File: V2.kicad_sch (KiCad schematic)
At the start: 106 parts, among them J5 Conn_01x06, Q1 NMOS, Q10 NMOS, Q11 NMOS, Q12 NMOS, Q13 Q_NPN_BCE, Q2 NMOS, Q3 NMOS, Q4 NMOS, Q5 NMOS, Q6 NMOS, Q7 NMOS, Q8 NMOS, Q9 NMOS, U10 STM32F042F6Px, U8 BQ25750RRVR, U9 BQ76952PFBR

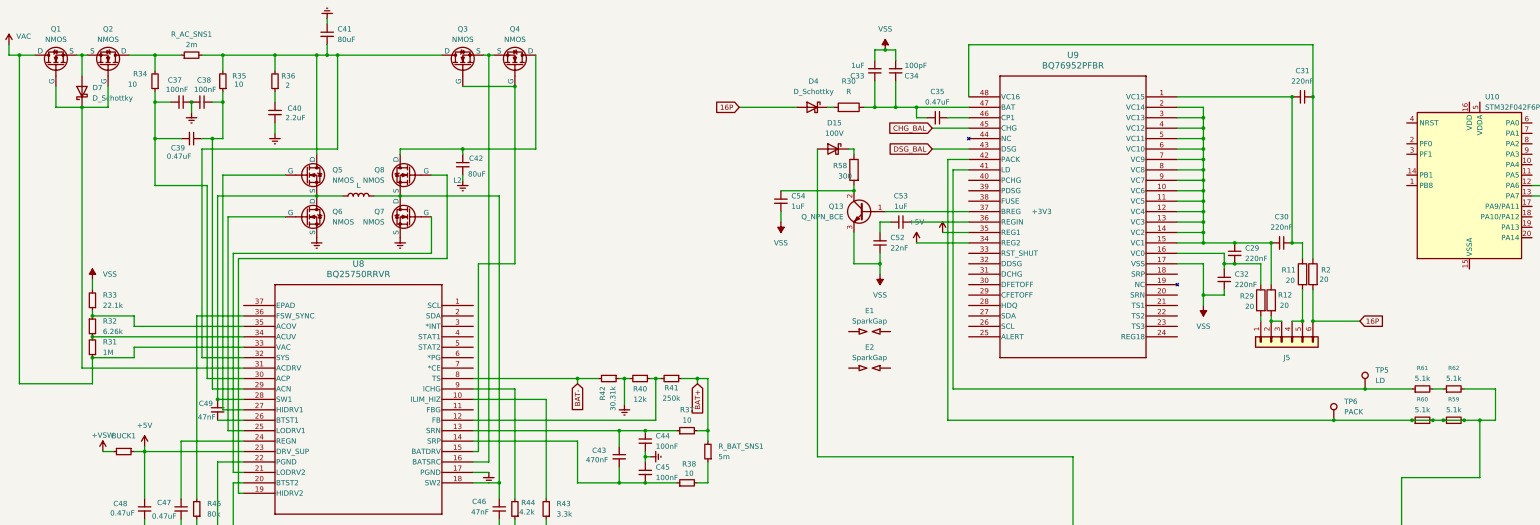
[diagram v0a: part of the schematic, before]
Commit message: Cell Balancer Reading Circuit cleaned up
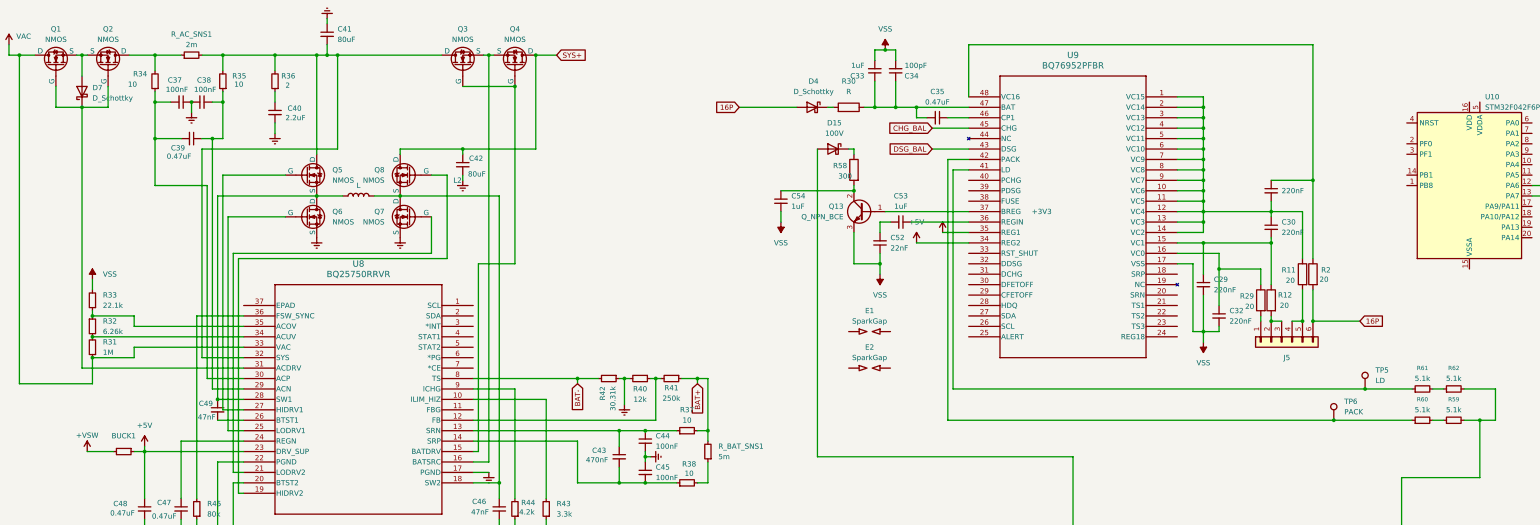
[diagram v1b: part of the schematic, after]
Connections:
- net BAT+: no longer R59.1, R60.1, R60.2, TP6.1, U9.42 (PACK)
- net VSS: now also C29.2
- net at C30.1, C31.2, R11.1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: now also U9.10 (VC6), U9.11 (VC5), U9.12 (VC4), U9.13 (VC3), U9.14 (VC2), U9.2 (VC14), U9.3 (VC13), U9.4 (VC12), U9.5 (VC11), U9.6 (VC10), U9.7 (VC9), U9.8 (VC8), U9.9 (VC7)
- net at C32.1, R29.1, U9.16 (VC0): no longer C29.2
- net SYS+: now reaches C42.1, Q4.1 (D), Q8.1 (D)
- new net: R60.1, TP6.1, U9.42 (PACK)
- new net: R59.1, R60.2
- new net: C29.1, C30.2, R12.1, U9.15 (VC1)
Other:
- moved on the sheet: C29, C30, C32

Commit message: Cleaned up
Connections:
- net BAT+: now also C42.1, Q4.1 (D), Q8.1 (D)
- net SYS+: now also C41.2, Q3.1 (D), Q5.1 (D), R35.2, R36.2, R_AC_SNS1.2, U8.32 (SYS); no longer C42.1, Q4.1 (D), Q8.1 (D)
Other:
- note added: "1 ist 1N 2 ist 1P 3 ist 2N (kurzgeschlossen mit 1P) 4 ist 2P 5 ist 3N (kurzgeschlossen mit 2P) 6 ist 3P"
- moved on the sheet: C30, J5, R11, R12, R2, R29

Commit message: Added MCU and connected relevant Pins
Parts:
- removed E1, E2: SparkGap, symbol Device:SparkGap
- removed J5: Conn_01x06, symbol Connector_Generic:Conn_01x06
- removed U10: STM32F042F6Px, Package_SO:TSSOP-20_4.4x6.5mm_P0.65mm, symbol MCU_ST_STM32F0:STM32F042F6Px
- added BT1, BT2, BT3: Battery_Cell, symbol Device:Battery_Cell
- added C57, C58: 10p, Capacitor_SMD:C_0603_1608Metric, symbol Device:C_Small
- added C59: 100n, Capacitor_SMD:C_0603_1608Metric, symbol Device:C_Small
- added J11: SWD Header, Connector_PinHeader_2.54mm:PinHeader_1x04_P2.54mm_Vertical, symbol Connector_Generic:Conn_01x04
- added J5, J6: Molex MicroFit 2x2, Connector_Molex:Molex_Micro-Fit_3.0_43045-0400_2x02_P3.00mm_Horizontal, symbol Connector_Generic:Conn_01x04
- added J8, J9: Molex MicroFit 2x3, Connector_Molex:Molex_Micro-Fit_3.0_43045-0600_2x03_P3.00mm_Horizontal, symbol Connector_Generic:Conn_01x06
- added JP2: r, Jumper:SolderJumper-2_P1.3mm_Open_RoundedPad1.0x1.5mm, symbol Jumper:SolderJumper_2_Open
- added R63: 120, DNP, Resistor_SMD:R_0603_1608Metric, symbol Device:R_Small
- added R64: 1k, Resistor_SMD:R_0603_1608Metric, symbol Device:R_Small
- added R65: 10k, Resistor_SMD:R_0603_1608Metric, symbol Device:R_Small
- added R66, R67: 4.7k, symbol Device:R
- added R68: 4.7k, symbol Device:R_Small
- added R69, R70, R71, R72: 5.1k, symbol Device:R_Small
- added U11: MCP2562-E-SN, Package_SO:SOIC-8_3.9x4.9mm_P1.27mm, symbol Interface_CAN_LIN:MCP2562-E-SN
- added U12: STM32F105RCTx, Package_QFP:LQFP-64_10x10mm_P0.5mm, symbol MCU_ST_STM32F1:STM32F105RCTx
- added Y2: 8MHz, 12p, Crystal:Crystal_SMD_5032-4Pin_5.0x3.2mm, symbol Device:Crystal_GND24
- D4: value D_Schottky -> 100V
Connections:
- net BAT+ is gone; now on net 3P: C42.1, C51.2, C55.2, D12.2 (A), D13.2 (A), E3.2, Q11.3 (S), Q12.3 (S), Q4.1 (D), Q8.1 (D), R37.2, R41.1, R55.1, R56.1, R59.2, R62.2, R_BAT_SNS1.2, TP3.1
- net +3V3: now also J11.1 (Pin_1), U11.5 (Vio)
- net +5V: now also U11.3 (VDD)
- net +VSW: now also J5.1 (Pin_1), J5.2 (Pin_2), J6.3 (Pin_3), J6.4 (Pin_4), J8.5 (Pin_5), J9.5 (Pin_5)
- net PGND: now also C37.1, C38.2, C40.2, C41.1, C42.2, C44.2, C45.1, C47.2, C48.2, Q6.3 (S), Q7.3 (S), R29.2, U8.17 (PGND), BT1.2 (-), J6.1 (Pin_1), J6.2 (Pin_2)
- net VSS: now also Q9.3 (S), R40.2, R42.1, R43.1, R44.1, R45.1, U8.22 (PGND), C57.1, C58.1, C59.1, JP2.2 (B), R65.1, R66.2, R67.2, R68.1, U11.2 (VSS), U12.18 (VSS), U12.31 (VSS), U12.47 (VSS), U12.63 (VSS), Y2.2, Y2.4
- net PACK: now reaches R60.1, TP6.1, U9.42 (PACK)
- net 2P: now reaches R11.2
- net 2P: now also BT2.1 (+), BT3.2 (-)
- net LD: now reaches R61.1, TP5.1, U9.41 (LD)
- net 1P: now reaches R12.2
- net 1P: now also BT1.1 (+), BT2.2 (-)
- net CD: now reaches D15.2 (A), Q10.1 (D), Q11.1 (D)
- net FUSE: now reaches R48.1
- net FUSE: now also U9.38 (FUSE)
- net ALERT_BAL: now reaches U9.25 (ALERT)
- net I2C_SCL: now reaches U9.26 (SCL)
- net I2C_SCL: now also U8.1 (SCL), R67.1, U12.61 (PB8)
- net I2C_SDA: now reaches U9.27 (SDA)
- net I2C_SDA: now also U8.2 (SDA), R66.1, U12.62 (PB9)
- net INT: now reaches U8.3 (*INT)
- net INT: now also R69.2, U12.25 (PC5)
- net STAT1: now reaches U8.4 (STAT1)
- net STAT1: now also R70.2, U12.37 (PC6)
- net STAT2: now reaches U8.5 (STAT2)
- net STAT2: now also R71.2, U12.38 (PC7)
- net PG: now reaches U8.6 (*PG)
- net PG: now also R72.2, U12.39 (PC8)
- net 16P renamed 3P
- net 3P: now also BT3.1 (+)
- removed net Earth: C37.1, C38.2, C40.2, C41.1, C42.2, C44.2, C45.1, C47.2, C48.2, Q6.3 (S), Q7.3 (S), R40.2, R42.1, R43.1, R44.1, R45.1, U8.17 (PGND), U8.22 (PGND)
- new net: C57.2, R64.2, Y2.1
- new net +3.3V: R69.1, R70.1, R71.1, R72.1
- new net +BATT: J5.3 (Pin_3), J5.4 (Pin_4)
- new net ALERT: U12.24 (PC4)
- new net BOOT: R65.2, U12.60 (BOOT0)
- new net CAN+: J8.6 (Pin_6), J9.6 (Pin_6), R63.1, U11.7 (CANH)
- new net CAN-: J8.3 (Pin_3), J9.3 (Pin_3), R63.2, U11.6 (CANL)
- new net CAN_RX: U11.4 (RXD), U12.44 (PA11)
- new net CAN_TX: U11.1 (TXD), U12.45 (PA12)
- new net GND: J11.4 (Pin_4), J8.1 (Pin_1), J8.2 (Pin_2), J9.1 (Pin_1), J9.2 (Pin_2), U11.8 (STBY)
- new net NRST: C59.2, JP2.1 (A), U12.7 (NRST)
- new net OSC_IN: R64.1, U12.3 (PC14)
- new net OSC_OUT: C58.2, U12.4 (PC15), Y2.3
- new net SWCLK: J11.3 (Pin_3), U12.49 (PA14)
- new net SWDIO: J11.2 (Pin_2), U12.46 (PA13)
- new net VDC: J8.4 (Pin_4), J9.4 (Pin_4)
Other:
- note added: "Back Side Connectors"
- note added: "Top Side Connectors"
- note removed: "1 ist 1N 2 ist 1P 3 ist 2N (kurzgeschlossen mit 1P) 4 ist 2P 5 ist 3N (kurzgeschlossen mit 2P) 6 ist 3P"
- moved on the sheet: C29, C30, C32, C33, C34, C35, C36, C50, C51, C52, C53, C54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

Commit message: :)
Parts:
- added C60: 470n, Capacitor_SMD:C_0603_1608Metric, symbol Device:C_Small
- added C61: 100n, Capacitor_SMD:C_0603_1608Metric, symbol Device:C_Small
- added U10: L7805, Package_TO_SOT_SMD:TO-252-2, symbol Regulator_Linear:L7805
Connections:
- net ALERT_BAL is gone; now on net ALERT: U9.25 (ALERT)
- net +5V: now also C61.1, U10.3 (OUT)
- net +VSW: now also C60.2, U10.1 (IN)
- net GND: now also C60.1, C61.2, U10.2 (GND)

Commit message: clean up
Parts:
- removed C59: 100n, Capacitor_SMD:C_0603_1608Metric, symbol Device:C_Small
- removed JP2: r, Jumper:SolderJumper-2_P1.3mm_Open_RoundedPad1.0x1.5mm, symbol Jumper:SolderJumper_2_Open
- removed R65: 10k, Resistor_SMD:R_0603_1608Metric, symbol Device:R_Small
- removed R71: 5.1k, symbol Device:R_Small
- removed Y2: 8MHz, 12p, Crystal:Crystal_SMD_5032-4Pin_5.0x3.2mm, symbol Device:Crystal_GND24
- added C62: 0.47uF, symbol Device:C_Small
- added C63: 100p, symbol Device:C_Small
- added C64: 0.1u, symbol Device:C_Small
- added C67: 4.7u, Capacitor_SMD:C_0402_1005Metric, symbol Device:C
- added C68, C69, C70, C71, C72: 100n, Capacitor_SMD:C_0402_1005Metric, symbol Device:C
- added C73, C76: 10n, Capacitor_SMD:C_0402_1005Metric, symbol Device:C
- added C74, C75: 1u, Capacitor_SMD:C_0402_1005Metric, symbol Device:C
- added C77, C78: 10p, Capacitor_SMD:C_0402_1005Metric, symbol Device:C
- added C79: 100n, Capacitor_SMD:C_0402_1005Metric, symbol Device:C_Small
- added C80: 22u, Capacitor_SMD:C_1206_3216Metric, symbol Device:C_Small
- added FB1: 120R, Inductor_SMD:L_0603_1608Metric, symbol Device:FerriteBead
- added J12: SWD Header, Connector_PinHeader_2.54mm:PinHeader_1x04_P2.54mm_Vertical, symbol Connector_Generic:Conn_01x04
- added NT1: NetTie_2, symbol Device:NetTie_2
- added R71, R78: 100, symbol Device:R
- added R73: 5.24k, symbol Device:R_Small
- added R74: 1k, Resistor_SMD:R_0402_1005Metric, symbol Device:R
- added R75: 1k, Resistor_SMD:R_0402_1005Metric, symbol Device:R_Small
- added R76: 100k, Resistor_SMD:R_0402_1005Metric, symbol Device:R_Small
- added R77: 0.001, symbol Device:R
- added SW1, SW2: KMR721NGLFS, Button_Switch_SMD:SW_Push_1P1T_NO_CK_KMR2, symbol Switch:SW_SPST
- added TP10, TP7, TP8, TP9: TestPoint, symbol Connector:TestPoint
- added TP11: BAT-, symbol Connector:TestPoint
- added U13: AZ1117I-3.3, Package_TO_SOT_SMD:SOT-223-3_TabPin2, symbol Regulator_Linear:AZ1117-3.3
- added Y3: 8MHz 12pF, Crystal:Crystal_SMD_5032-4Pin_5.0x3.2mm, symbol Device:Crystal_GND24
- C39: value 0.47uF -> 470n
- C57: value 10p -> 2.2u; footprint Capacitor_SMD:C_0603_1608Metric -> (none); LCSC# C1634 -> (none); Manufacturer Samsung Electro-Mechanics -> (none); Part# CL10C100JB8NNNC -> (none)
- C58: value 10p -> 470n; LCSC# C1634 -> C1623; Part# CL10C100JB8NNNC -> CL10B474KA8NNNC
- C60: value 470n -> 100n; LCSC# C1623 -> C14663; Manufacturer Samsung Electro-Mechanics -> YAGEO; Part# CL10B474KA8NNNC -> CC0603KRX7R9BB104
- C61: value 100n -> 10u; footprint Capacitor_SMD:C_0603_1608Metric -> Capacitor_SMD:C_1206_3216Metric; LCSC# C14663 -> C13585; Manufacturer YAGEO -> Samsung Electro-Mechanics; Part# CC0603KRX7R9BB104 -> CL31A106KBHNNNE
- R30: value R -> 100
- R31: value 1M -> 1k
- R64: value 1k -> 10k; footprint Resistor_SMD:R_0603_1608Metric -> (none); LCSC# C21190 -> (none); Manufacturer UNI-ROYAL(Uniroyal Elec) -> (none); Part# 0603WAF1001T5E -> (none)
- R69, R70, R72: value 5.1k -> 10k
- TP5: value LD -> PACK
- TP6: value PACK -> LD
- U9: Technical Reference Manual (none) -> https://www.ti.com/lit/ug/sluuby2b/sluuby2b.pdf?ts=17468710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
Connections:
- net SYS+ is gone; now on net PRE_OUT: C41.2, Q3.1 (D), Q5.1 (D), R35.2, R36.2, R_AC_SNS1.2, U8.32 (SYS)
- net +3.3V: now also R64.1, R66.2, R67.2, U12.1 (VBAT), U12.19 (VDD), U12.32 (VDD), U12.48 (VDD), U12.64 (VDD), C67.1, C68.1, C69.1, C70.1, C71.1, C72.1, C75.1, C76.1, FB1.1, R75.2
- net +3V3: now also C80.2, J12.1 (Pin_1), U13.2 (VO); no longer U9.35 (REG1)
- net +5V: now also C60.1, C61.2, U13.3 (VI); no longer C61.1, U9.34 (REG2)
- net +VSW: now also C58.2; no longer C60.2
- net 3P: no longer C42.1, Q4.1 (D), Q8.1 (D)
- net ALERT: now also R68.2
- net BOOT: now also R76.2, SW1.1 (A)
- net GND: now also C58.1, C60.2, C61.1, C67.2, C68.2, C69.2, C70.2, C71.2, C72.2, C73.2, C74.2, C75.2, C76.2, C77.2, C78.2, C79.1, C80.1, J12.4 (Pin_4), R76.1, SW2.1 (A), U13.1 (GND), Y3.2, Y3.4; no longer C60.1, C61.2
- net I2C_SCL: now also J12.2 (Pin_2)
- net I2C_SDA: now also J12.3 (Pin_3)
- net INT: now also R72.2; no longer R69.2
- net LD: now also R60.1, TP6.1; no longer R61.1, TP5.1
- net NRST: now also C79.2, SW2.2 (B)
- net PACK: now also R61.1, TP5.1; no longer R60.1, TP6.1
- net PG: now also R69.2; no longer R72.2
- net PGND: now also C29.2, C32.2, C33.1, C34.1, C36.2, C52.1, C53.2, C54.2, C57.2, D9.2 (A), Q9.3 (S), R33.1, R40.1, R42.1, R43.1, R44.1, R45.1, R47.2, R68.1, U11.2 (VSS), U12.12 (VSSA), U12.18 (VSS), U12.31 (VSS), U12.47 (VSS), U12.63 (VSS), U8.22 (PGND), U8.37 (EPAD), U9.17 (VSS), C62.2, NT1.1, NT1.2, R71.1, R73.2, R77.1, R77.2, R78.1, TP11.1, TP8.1
- net STAT1: now also R64.2; no longer R70.2
- net STAT2: now also R70.2
- net VDC: now also Q1.1 (D), R31.2, U8.33 (VAC), C62.1
- net at D12.1 (K): now also D14.1 (K), Q12.1 (D), R51.2, R52.1, R53.1, R55.2, R57.2, TP4.1
- net REGN: now reaches C47.1, U8.24 (REGN)
- net REGN: now also R73.1
- net at C52.2: now also Q13.3 (E), U9.36 (REGIN); no longer C53.2
- net ACN: now reaches C38.1, C39.1, R35.1, U8.29 (ACN)
- net ACP: now reaches C37.2, C39.2, R34.1, U8.30 (ACP)
- net at C53.1: now also U9.35 (REG1); no longer U9.36 (REGIN)
- net at R41.2, U8.12 (FB): now also C42.1, Q4.1 (D), Q8.1 (D), R40.2; no longer R40.1
- net at C35.2, R30.1, U9.47 (BAT): now also C33.2, C34.2; no longer C33.1, C34.1
- net +3.3VA: now reaches U12.13 (VDDA)
- net +3.3VA: now also C73.1, C74.1, FB1.2
- net RST_SHUT: now reaches U12.16 (PA2)
- net RST_SHUT: now also U9.33 (RST_SHUT)
- net TS2: now reaches U12.17 (PA3)
- net TS2: now also U9.22 (TS2)
- net HSE_IN: now reaches U12.5 (PD0)
- net HSE_IN: now also C78.1, Y3.3
- net HSE_OUT: now reaches U12.6 (PD1)
- net HSE_OUT: now also R74.1
- net HIDRV2: now reaches Q8.2 (G), U8.19 (HIDRV2)
- net HIDRV2: now also Q5.2 (G)
- net SW2: now reaches C46.1, L2.2, Q7.1 (D), Q8.3 (S), U8.18 (SW2)
- net SW1: now reaches C49.1, L2.1, Q5.3 (S), Q6.1 (D), U8.28 (SW1)
- net BTST1: now reaches C49.2, U8.26 (BTST1)
- net HIDRV1: now reaches U8.27 (HIDRV1)
- net HIDRV1: no longer Q5.2 (G)
- net BATDRV: now reaches Q3.2 (G), Q4.2 (G), U8.15 (BATDRV)
- net BATSRC: now reaches Q3.3 (S), Q4.3 (S), U8.16 (BATSRC)
- net BTST2: now reaches C46.2, U8.20 (BTST2)
- net LODRV2: now reaches Q7.2 (G), U8.21 (LODRV2)
- net LODRV1: now reaches Q6.2 (G), U8.25 (LODRV1)
- net at U9.18 (SRP): now also C63.2, C64.2, R71.2, TP9.1
- net at U9.20 (SRN): now also C63.1, C64.1, R78.2, TP10.1
- net at U9.24 (REG18): now also C57.1, TP7.1
- net +BATT renamed PRE_OUT
- net OSC_IN: no longer names the net of U12.3 (PC14)
- net OSC_IN: no longer R64.1
- net OSC_OUT: no longer names the net of U12.4 (PC15)
- net OSC_OUT: no longer C58.2
- removed net VAC: Q1.1 (D), R31.1, U8.33 (VAC)
- removed net VSS: C29.2, C32.2, C33.2, C34.2, C36.2, C52.1, C54.2, C57.1, C58.1, D9.2 (A), Q13.3 (E), Q9.3 (S), R33.2, R40.2, R42.1, R43.1, R44.1, R45.1, R47.2, R66.2, R67.2, R68.1, U11.2 (VSS), U12.18 (VSS), U12.31 (VSS), U12.47 (VSS), U12.63 (VSS), U8.22 (PGND), U9.17 (VSS)
- new net: C77.1, R74.2, Y3.1
- new net: R75.1, SW1.2 (B)
- new net ACOV: R32.2, R33.2, U8.35 (ACOV)
- new net ACUV: R31.1, R32.1, U8.34 (ACUV)
- no-connect marks 0 -> 46
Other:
- note added: "12.6V"
- note added: "@TODO connect to REGN"
- note added: "@todo herausfinden wie man REGIn programmiert ohne vorher den MCU zu grillen"
- note added: "Additional Circuitry for bq76952"
- note added: "CAN"
- note added: "Charge Bus?"
- note added: "Connector to enable the power put. To enable VSW, short PRE_OUT and +VSW"
- note added: "FBG: connect to the bottom of battery feedback resistor CE: Active Low Charge Enable Pin: do not leave floating: -> mit STM32 verbinden -> Spannung kontrollieren EPAD: Kühlung. Verbinden mit Kupferplatte"
- note added: "Formel auf Seite 64 checken und Widerstände anpassen"
- note added: "REG1 and REG2 can be configured to provide power to external stuff The voltage level can be controlled via registers of the chip (with one-time-programmable or at runtime)"
- note added: "REG1 und REG 2 doch irgonieren und extra regultor für STM32 nutzen?"
- note added: "RST_SHUT: To reset the chip (@TODO check if this works) TS2: needed to wake the chip again after it enterted SHUTDOWNMODE"
- note added: "Regulator"
- note added: "SRN und SRP: Messen wie viel Ampersekunden durch die Batterie geflossen ist"
- note added: "There are two grounds: - PGND: is for the high power rail - GND: for every other component"
- note added: "Verbraucher hier anschießen"
- note added: "Was machen Q9 und Q12? Sollten wir Q10 und Q11 weglassen?"
- note added: "connect INT, STAT1, STAT2 and PG to a logic rail via 10k resistor (bq25750 man. page 5)"
- company: (none) -> TUDSaT
- title: (none) -> Rapid Power Module (mark III)
- moved on the sheet: BT1, BT2, BT3, BUCK1, C29, C30, C32, C33, C34, C35, C36, C37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

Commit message: more cleanup
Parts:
- removed R31: 1k, symbol Device:R_Small
- removed R32: 6.26k, symbol Device:R_Small
- removed R33: 22.1k, symbol Device:R_Small
- removed R36: 2, symbol Device:R_Small
- removed R37, R38: 10, symbol Device:R_Small
- removed R40: 12k, symbol Device:R_Small
- removed R41: 250k, symbol Device:R_Small
- removed R42: 30.31k, symbol Device:R_Small
- removed R43: 3.3k, symbol Device:R_Small
- removed R44: 4.2k, symbol Device:R_Small
- removed R45: 80k, symbol Device:R_Small
- removed R63: 120, DNP, Resistor_SMD:R_0603_1608Metric, symbol Device:R_Small
- removed R73: 5.24k, symbol Device:R_Small
- removed R75: 1k, Resistor_SMD:R_0402_1005Metric, symbol Device:R_Small
- removed R_AC_SNS1: 2m, symbol Device:R_Small
- removed R_BAT_SNS1: 5m, symbol Device:R_Small
- added R31: 80k, Resistor_SMD:R_0603_1608Metric, symbol Device:R
- added R32: 5k24, Resistor_SMD:R_0603_1608Metric, symbol Device:R
- added R33: 6k26, Resistor_SMD:R_0603_1608Metric, symbol Device:R
- added R36: 250k, Resistor_SMD:R_0603_1608Metric, symbol Device:R
- added R37, R41, R79, R80: 10, Resistor_SMD:R_0603_1608Metric, symbol Device:R
- added R38: 5m, symbol Device:R
- added R40: 3k3, Resistor_SMD:R_0603_1608Metric, symbol Device:R
- added R42: 12k, Resistor_SMD:R_0603_1608Metric, symbol Device:R
- added R43: 22k1, Resistor_SMD:R_0603_1608Metric, symbol Device:R
- added R44: 1k, Resistor_SMD:R_0603_1608Metric, symbol Device:R
- added R65: 2m, symbol Device:R
- added R81: 2, Resistor_SMD:R_0603_1608Metric, symbol Device:R
- added R82: 30k31, Resistor_SMD:R_0603_1608Metric, symbol Device:R
- added R83: 4k2, Resistor_SMD:R_0603_1608Metric, symbol Device:R
- C29, C30, C31, C32: value 220nF -> 220n; footprint (none) -> Capacitor_SMD:C_0603_1608Metric
- C33: value 1uF -> 1u; footprint (none) -> Capacitor_SMD:C_1206_3216Metric
- C34: value 100pF -> 100p; footprint (none) -> Capacitor_SMD:C_0603_1608Metric
- C35, C47, C48: value 0.47uF -> 470n; footprint (none) -> Capacitor_SMD:C_0603_1608Metric
- C36, C50, C51, C55, C56: value 0.1uF -> 100n; footprint (none) -> Capacitor_SMD:C_0603_1608Metric
- C37, C38, C44, C45: value 100nF -> 100n; footprint (none) -> Capacitor_SMD:C_0603_1608Metric
- C39, C63, R11, R12: footprint (none) -> Capacitor_SMD:C_0603_1608Metric
- C40: value 2.2uF -> 2u2; footprint (none) -> Capacitor_SMD:C_1206_3216Metric
- C41, C42: value 80uF -> 80u; footprint (none) -> Capacitor_SMD:C_1206_3216Metric
- C43: value 470nF -> 470n; footprint (none) -> Capacitor_SMD:C_0603_1608Metric
- C46, C49: value 47nF -> 47n; footprint (none) -> Capacitor_SMD:C_0603_1608Metric
- C52: value 22nF -> 22n; footprint (none) -> Capacitor_SMD:C_0603_1608Metric
- C53, C54, C57, C62: footprint (none) -> Capacitor_SMD:C_1206_3216Metric
- C64: value 0.1u -> 100n; footprint (none) -> Capacitor_SMD:C_0603_1608Metric
- C67: value 4.7u -> 4u7
- R29, R30, R47, R48, R50, R51, R59, R60, R61, R62, R64, R66, R67, R69, R70, R71, R72, R77, R78: footprint (none) -> Resistor_SMD:R_0603_1608Metric
- R34: value 10 -> 1k; footprint (none) -> Resistor_SMD:R_0603_1608Metric
- R35: value 10 -> 120; footprint (none) -> Resistor_SMD:R_0603_1608Metric
- R39, R46, R53: value 7.5k -> 7k5; footprint (none) -> Resistor_SMD:R_0603_1608Metric
- R52, R54: value 5.1k -> 5k1; footprint (none) -> Resistor_SMD:R_0603_1608Metric
- R68: value 4.7k -> 4k7; footprint (none) -> Resistor_SMD:R_0603_1608Metric
- U8: footprint VQFN36_RRV_TEX -> bq25750:VQFN36_RRV_TEX
- U9: footprint QFP_2PFBR_TEX -> bq76952:QFP_2PFBR_TEX
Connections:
- net GND is gone; now on net PGND: C58.1, C60.2, C61.1, C67.2, C68.2, C69.2, C70.2, C71.2, C72.2, C73.2, C74.2, C75.2, C76.2, C77.2, C78.2, C79.1, C80.1, J11.4 (Pin_4), J12.4 (Pin_4), J8.1 (Pin_1), J8.2 (Pin_2), J9.1 (Pin_1), J9.2 (Pin_2), R76.1, SW2.1 (A), U10.2 (GND), U11.8 (STBY), U13.1 (GND), Y3.2, Y3.4
- net +3.3V: no longer C67.1, C68.1, C69.1, C70.1, C71.1, C72.1, C75.1, C76.1, FB1.1, R66.2, R67.2, U12.1 (VBAT), U12.19 (VDD), U12.32 (VDD), U12.48 (VDD), U12.64 (VDD)
- net +3V3: now also C67.1, C68.1, C69.1, C70.1, C71.1, C72.1, C75.1, C76.1, FB1.1, R34.1, R66.2, R67.2, U12.1 (VBAT), U12.19 (VDD), U12.32 (VDD), U12.48 (VDD), U12.64 (VDD)
- net 3P: now also R36.2, R38.1, R41.2
- net ACN: now also R79.2; no longer R35.1
- net ACOV: now also R33.2, R43.1
- net ACP: now also R80.2; no longer R34.1
- net ACUV: now also R33.1, R44.2
- net CAN+: now also R35.1
- net CAN-: now also R35.2
- net HIDRV1: now also Q5.2 (G)
- net HIDRV2: no longer Q5.2 (G)
- net PGND: now also R31.2, R32.1, R40.2, R42.2, R43.2, R82.1, R82.2, R83.2
- net PRE_OUT: now also R65.2, R79.1, R81.1; no longer R35.2
- net REGN: now also R32.2
- net VDC: now also R44.1
- net at Q2.1 (D): now also R65.1, R80.1; no longer R34.2
- net at C43.1, C44.1, U8.13 (SRN): now also R41.1
- net at C42.1, Q4.1 (D), Q8.1 (D)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: now also R36.1, R42.1
- net at U8.36 (FSW_SYNC): now also R31.1
- net at C40.1: now also R81.2
- net at U8.10 (ILIM_HIZ): now also R40.1
- net at SW1.2 (B): now also R34.2
- net at C43.2, C45.2, U8.14 (SRP): now also R37.1
- net at U8.9 (ICHG): now also R83.1
- net +3.3VA renamed +3VA3
- new net: R37.2, R38.2
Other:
- note added: "DNP"
- note added: "R_AC_SNS1"
- note added: "R_BAT_SNS1"
